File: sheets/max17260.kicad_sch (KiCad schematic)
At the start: 4 parts, among them U7 MAX17260

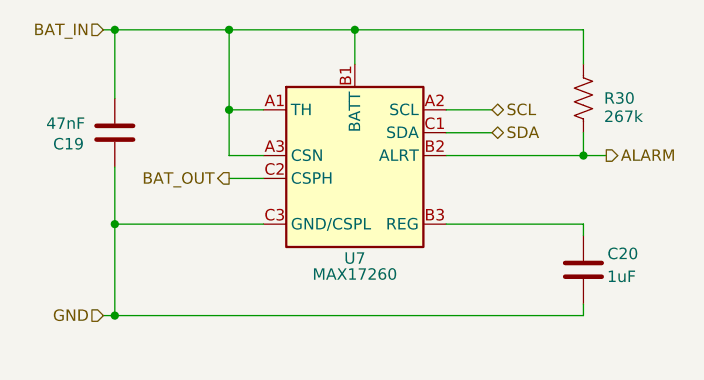
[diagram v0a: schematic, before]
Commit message: Change max17260 footprint
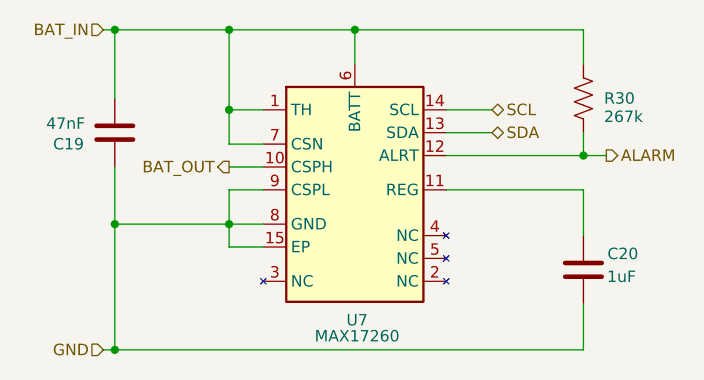
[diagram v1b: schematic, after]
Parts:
- U7: footprint Package_BGA:WLP-9_1.448x1.468mm_Layout3x3_P0.4mm_Ball0.27mm_Pad0.25mm -> Package_DFN_QFN:TDFN-14-1EP_3x3mm_P0.4mm_EP1.78x2.35mm
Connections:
- net ALARM: now also U7.12 (ALRT); no longer U7.B2 (ALRT)
- net BAT_IN: now also U7.1 (TH), U7.6 (BATT), U7.7 (CSN); no longer U7.A1 (TH), U7.A3 (CSN), U7.B1 (BATT)
- net BAT_OUT: now also U7.10 (CSPH); no longer U7.C2 (CSPH)
- net GND: now also U7.15 (EP), U7.8 (GND), U7.9 (CSPL); no longer U7.C3 (GND/CSPL)
- net SCL: now also U7.14 (SCL); no longer U7.A2 (SCL)
- net SDA: now also U7.13 (SDA); no longer U7.C1 (SDA)
- net at C20.1: now also U7.11 (REG); no longer U7.B3 (REG)
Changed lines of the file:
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@@
 	)
 	(junction
-		(at 78.74 83.82)
+		(at 78.74 87.63)
 		(diameter 0)
 		(color 0 0 0 0)
@@
 	)
 	(junction
+		(at 91.44 73.66)
+		(diameter 0)
+		(color 0 0 0 0)
+	)
+	(junction
 		(at 91.44 60.96)
 		(diameter 0)
@@
 	(wire
 		(pts
-			(xy 130.81 73.66) (xy 130.81 74.93)
+			(xy 95.25 69.85) (xy 91.44 69.85)
+		)
+		(stroke
+			(width 0)
+			(type default)
+		)
+	)
+	(wire
+		(pts
+			(xy 130.81 69.85) (xy 130.81 74.93)
+		)
+		(stroke
+			(width 0)
+			(type default)
+		)
+	)
+	(wire
+		(pts
+			(xy 115.57 66.04) (xy 130.81 66.04)
 		)
 		(stroke
@@
 	(wire
 		(pts
+			(xy 91.44 76.2) (xy 91.44 73.66)
+		)
+		(stroke
+			(width 0)
+			(type default)
+		)
+	)
+	(wire
+		(pts
 			(xy 115.57 63.5) (xy 120.65 63.5)
 		)
@@
 	(wire
 		(pts
+			(xy 77.47 52.07) (xy 78.74 52.07)
+		)
+		(stroke
+			(width 0)
+			(type default)
+		)
+	)
+	(wire
+		(pts
+			(xy 78.74 59.69) (xy 78.74 52.07)
+		)
+		(stroke
+			(width 0)
+			(type default)
+		)
+	)
+	(wire
+		(pts
+			(xy 91.44 67.31) (xy 95.25 67.31)
+		)
+		(stroke
+			(width 0)
+			(type default)
+		)
+	)
+	(wire
+		(pts
+			(xy 91.44 73.66) (xy 95.25 73.66)
+		)
+		(stroke
+			(width 0)
+			(type default)
+		)
+	)
+	(wire
+		(pts
+			(xy 130.81 66.04) (xy 133.35 66.04)
+		)
+		(stroke
+			(width 0)
+			(type default)
+		)
+	)
+	(wire
+		(pts
+			(xy 78.74 73.66) (xy 78.74 67.31)
+		)
+		(stroke
+			(width 0)
+			(type default)
+		)
+	)
+	(wire
+		(pts
+			(xy 130.81 87.63) (xy 130.81 82.55)
+		)
+		(stroke
+			(width 0)
+			(type default)
+		)
+	)
+	(wire
+		(pts
+			(xy 91.44 52.07) (xy 105.41 52.07)
+		)
+		(stroke
+			(width 0)
+			(type default)
+		)
+	)
+	(wire
+		(pts
 			(xy 91.44 60.96) (xy 95.25 60.96)
 		)
@@
 	(wire
 		(pts
-			(xy 77.47 52.07) (xy 78.74 52.07)
-		)
-		(stroke
-			(width 0)
-			(type default)
-		)
-	)
-	(wire
-		(pts
-			(xy 78.74 59.69) (xy 78.74 52.07)
-		)
-		(stroke
-			(width 0)
-			(type default)
-		)
-	)
-	(wire
-		(pts
-			(xy 91.44 68.58) (xy 95.25 68.58)
-		)
-		(stroke
-			(width 0)
-			(type default)
-		)
-	)
-	(wire
-		(pts
-			(xy 130.81 66.04) (xy 133.35 66.04)
-		)
-		(stroke
-			(width 0)
-			(type default)
-		)
-	)
-	(wire
-		(pts
-			(xy 78.74 73.66) (xy 78.74 67.31)
-		)
-		(stroke
-			(width 0)
-			(type default)
-		)
-	)
-	(wire
-		(pts
-			(xy 130.81 83.82) (xy 130.81 82.55)
-		)
-		(stroke
-			(width 0)
-			(type default)
-		)
-	)
-	(wire
-		(pts
-			(xy 91.44 52.07) (xy 105.41 52.07)
+			(xy 91.44 69.85) (xy 91.44 73.66)
+		)
+		(stroke
+			(width 0)
+			(type default)
+		)
+	)
+	(wire
+		(pts
+			(xy 91.44 64.77) (xy 95.25 64.77)
+		)
+		(stroke
+			(width 0)
+			(type default)
+		)
+	)
+	(wire
+		(pts
+			(xy 91.44 73.66) (xy 78.74 73.66)
+		)
+		(stroke
+			(width 0)
+			(type default)
+		)
+	)
+	(wire
+		(pts
+			(xy 105.41 52.07) (xy 130.81 52.07)
 		)
 		(stroke
@@
 	(wire
 		(pts
-			(xy 91.44 66.04) (xy 95.25 66.04)
-		)
-		(stroke
-			(width 0)
-			(type default)
-		)
-	)
-	(wire
-		(pts
-			(xy 115.57 66.04) (xy 130.81 66.04)
-		)
-		(stroke
-			(width 0)
-			(type default)
-		)
-	)
-	(wire
-		(pts
-			(xy 105.41 52.07) (xy 130.81 52.07)
-		)
-		(stroke
-			(width 0)
-			(type default)
-		)
-	)
-	(wire
-		(pts
-			(xy 91.44 60.96) (xy 91.44 66.04)
-		)
-		(stroke
-			(width 0)
-			(type default)
-		)
-	)
-	(wire
-		(pts
 			(xy 78.74 52.07) (xy 91.44 52.07)
 		)
@@
 	(wire
 		(pts
-			(xy 130.81 83.82) (xy 78.74 83.82)
-		)
-		(stroke
-			(width 0)
-			(type default)
-		)
-	)
-	(wire
-		(pts
-			(xy 115.57 73.66) (xy 130.81 73.66)
-		)
-		(stroke
-			(width 0)
-			(type default)
-		)
-	)
-	(wire
-		(pts
-			(xy 77.47 83.82) (xy 78.74 83.82)
+			(xy 130.81 87.63) (xy 78.74 87.63)
+		)
+		(stroke
+			(width 0)
+			(type default)
+		)
+	)
+	(wire
+		(pts
+			(xy 115.57 69.85) (xy 130.81 69.85)
+		)
+		(stroke
+			(width 0)
+			(type default)
+		)
+	)
+	(wire
+		(pts
+			(xy 77.47 87.63) (xy 78.74 87.63)
 		)
 		(stroke
@@
 	(wire
 		(pts
-			(xy 78.74 83.82) (xy 78.74 73.66)
-		)
-		(stroke
-			(width 0)
-			(type default)
-		)
-	)
-	(wire
-		(pts
-			(xy 95.25 73.66) (xy 78.74 73.66)
+			(xy 78.74 87.63) (xy 78.74 73.66)
 		)
 		(stroke
@@
 		(pts
 			(xy 105.41 55.88) (xy 105.41 52.07)
+		)
+		(stroke
+			(width 0)
+			(type default)
+		)
+	)
+	(wire
+		(pts
+			(xy 95.25 76.2) (xy 91.44 76.2)
+		)
+		(stroke
+			(width 0)
+			(type default)
+		)
+	)
+	(wire
+		(pts
+			(xy 91.44 60.96) (xy 91.44 64.77)
 		)
 		(stroke
@@
 	(hierarchical_label "GND"
 		(shape input)
-		(at 77.47 83.82 180)
+		(at 77.47 87.63 180)
 		(fields_autoplaced yes)
 		(effects
@@
 	(hierarchical_label "BAT_OUT"
 		(shape output)
-		(at 91.44 68.58 180)
+		(at 91.44 67.31 180)
 		(fields_autoplaced yes)
 		(effects
@@
 	(symbol
 		(lib_id "PowerFeather_KiCAD_Lib:MAX17260")
-		(at 105.41 67.31 0)
+		(at 105.41 69.85 0)
 		(unit 1)
 		(exclude_from_sim no)
@@
 		(dnp no)
 		(property "Reference" "U7"
-			(at 105.41 77.47 0)
+			(at 105.664 84.328 0)
 			(effects
 				(font
@@
 		)
 		(property "Value" "MAX17260"
-			(at 105.41 79.248 0)
-			(effects
-				(font
-					(size 1.27 1.27)
-				)
-			)
-		)
-		(property "Footprint" "Package_BGA:WLP-9_1.448x1.468mm_Layout3x3_P0.4mm_Ball0.27mm_Pad0.25mm"
-			(at 105.41 77.978 0)
+			(at 105.664 86.106 0)
+			(effects
+				(font
+					(size 1.27 1.27)
+				)
+			)
+		)
+		(property "Footprint" "Package_DFN_QFN:TDFN-14-1EP_3x3mm_P0.4mm_EP1.78x2.35mm"
+			(at 105.41 80.518 0)
 			(effects
 				(font
@@
 		)
 		(property "Datasheet" "https://www.mouser.com/datasheet/2/609/MAX17260-3469057.pdf"
-			(at 104.648 80.518 0)
+			(at 104.648 83.058 0)
 			(effects
 				(font
@@
 		)
 		(property "Description" ""
-			(at 105.41 67.31 0)
+			(at 105.41 69.85 0)
 			(effects
 				(font
@@
 		)
 		(property "MPN" "700-MAX17260BEWL+T"
-			(at 105.41 67.31 0)
-			(effects
-				(font
-					(size 1.27 1.27)
-				)
-				(hide yes)
-			)
-		)
-		(pin "C3"
-		)
-		(pin "A1"
-		)
-		(pin "B3"
-		)
-		(pin "B1"
-		)
-		(pin "A2"
-		)
-		(pin "C1"
-		)
-		(pin "B2"
-		)
-		(pin "A3"
-		)
-		(pin "C2"
+			(at 105.41 69.85 0)
+			(effects
+				(font
+					(size 1.27 1.27)
+				)
+				(hide yes)
+			)
+		)
+		(pin "14"
+		)
+		(pin "5"
+		)
+		(pin "11"
+		)
+		(pin "13"
+		)
+		(pin "3"
+		)
+		(pin "1"
+		)
+		(pin "10"
+		)
+		(pin "9"
+		)
+		(pin "4"
+		)
+		(pin "7"
+		)
+		(pin "8"
+		)
+		(pin "2"
+		)
+		(pin "6"
+		)
+		(pin "12"
+		)
+		(pin "15"
 		)
 		(instances

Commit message: Add VPU to max17260
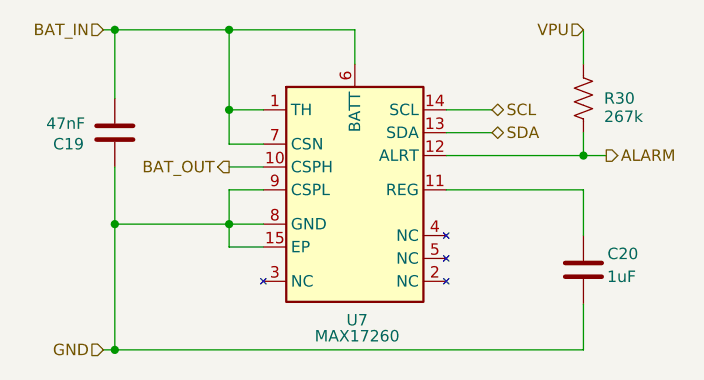
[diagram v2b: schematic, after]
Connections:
- net BAT_IN: no longer R30.1
- new net VPU: R30.1
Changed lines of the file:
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@@
-	)
-	(junction
-		(at 105.41 52.07)
-		(diameter 0)
-		(color 0 0 0 0)
 	)
 	(junction
@@
 		(pts
 			(xy 91.44 73.66) (xy 78.74 73.66)
-		)
-		(stroke
-			(width 0)
-			(type default)
-		)
-	)
-	(wire
-		(pts
-			(xy 105.41 52.07) (xy 130.81 52.07)
 		)
 		(stroke
@@
 		(fields_autoplaced yes)
 		(effects
+			(font
+				(size 1.27 1.27)
+			)
+			(justify right)
+		)
+	)
+	(hierarchical_label "VPU"
+		(shape input)
+		(at 130.81 52.07 180)
+		(fields_autoplaced yes)
+		(effects

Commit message: Change out values of some parts
- Fix max17260 sku
- Use 800 ohms for stat pin
- Change charger inductor value
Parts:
- U7: MPN 700-MAX17260BEWL+T -> 700-MAX17260SETD+T
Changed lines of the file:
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@@
 			)
 		)
-		(property "MPN" "700-MAX17260BEWL+T"
+		(property "MPN" "700-MAX17260SETD+T"
 			(at 105.41 69.85 0)
 			(effects
